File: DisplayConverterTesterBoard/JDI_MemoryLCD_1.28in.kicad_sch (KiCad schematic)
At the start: 6 parts, among them J6 Conn_01x03, J7 Conn_01x10_MountingPin

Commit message: set components LCSC
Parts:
- C? (x2): footprint (none) -> Capacitor_SMD:C_0805_2012Metric_Pad1.18x1.45mm_HandSolder; LCSC (none) -> C1853551; Vendor (none) -> YAGEO(国巨); Vendor Model (none) -> CC0805JKX7R0BB104
- C?: footprint (none) -> Resistor_SMD:R_0805_2012Metric_Pad1.20x1.40mm_HandSolder; LCSC (none) -> C28323; Vendor (none) -> SAMSUNG(三星); Vendor Model (none) -> CL21B105KBFNNNE
- NT2: footprint (none) -> NetTie:NetTie-3_SMD_Pad0.5mm
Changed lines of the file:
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@@
       (effects (font (size 1.27 1.27)) (justify left))
     )
-    (property "Footprint" "" (at 143.2052 138.43 0)
+    (property "Footprint" "Capacitor_SMD:C_0805_2012Metric_Pad1.18x1.45mm_HandSolder" (at 143.2052 138.43 0)
       (effects (font (size 1.27 1.27)) hide)
     )
     (property "Datasheet" "~" (at 142.24 134.62 0)
+      (effects (font (size 1.27 1.27)) hide)
+    )
+    (property "Description" "容值: 100nF 精度: ±5% 额定电压: 100V 材质(温度系数): X7R " (at 142.24 134.62 0)
+      (effects (font (size 1.27 1.27)) hide)
+    )
+    (property "LCSC" "C1853551" (at 142.24 134.62 0)
+      (effects (font (size 1.27 1.27)) hide)
+    )
+    (property "Vendor" "YAGEO(国巨)" (at 142.24 134.62 0)
+      (effects (font (size 1.27 1.27)) hide)
+    )
+    (property "Vendor Model" "CC0805JKX7R0BB104" (at 142.24 134.62 0)
       (effects (font (size 1.27 1.27)) hide)
     )
@@
       (effects (font (size 1.27 1.27)))
     )
-    (property "Footprint" "" (at 140.97 170.18 0)
+    (property "Footprint" "NetTie:NetTie-3_SMD_Pad0.5mm" (at 140.97 170.18 0)
       (effects (font (size 1.27 1.27)) hide)
     )
@@
       (effects (font (size 1.27 1.27)) hide)
     )
+    (property "Description" "" (at 140.97 170.18 0)
+      (effects (font (size 1.27 1.27)) hide)
+    )
+    (property "LCSC" "" (at 140.97 170.18 0)
+      (effects (font (size 1.27 1.27)) hide)
+    )
+    (property "Vendor" "" (at 140.97 170.18 0)
+      (effects (font (size 1.27 1.27)) hide)
+    )
+    (property "Vendor Model" "" (at 140.97 170.18 0)
+      (effects (font (size 1.27 1.27)) hide)
+    )
     (pin "1")
     (pin "2")
@@
     )
     (property "Datasheet" "~" (at 67.31 83.82 0)
+      (effects (font (size 1.27 1.27)) hide)
+    )
+    (property "Description" "" (at 67.31 83.82 0)
+      (effects (font (size 1.27 1.27)) hide)
+    )
+    (property "LCSC" "" (at 67.31 83.82 0)
+      (effects (font (size 1.27 1.27)) hide)
+    )
+    (property "Vendor" "" (at 67.31 83.82 0)
+      (effects (font (size 1.27 1.27)) hide)
+    )
+    (property "Vendor Model" "" (at 67.31 83.82 0)
       (effects (font (size 1.27 1.27)) hide)
     )
@@
       (effects (font (size 1.27 1.27)) (justify left))
     )
-    (property "Footprint" "" (at 159.7152 138.43 0)
+    (property "Footprint" "Capacitor_SMD:C_0805_2012Metric_Pad1.18x1.45mm_HandSolder" (at 159.7152 138.43 0)
       (effects (font (size 1.27 1.27)) hide)
     )
     (property "Datasheet" "~" (at 158.75 134.62 0)
+      (effects (font (size 1.27 1.27)) hide)
+    )
+    (property "Description" "容值: 100nF 精度: ±5% 额定电压: 100V 材质(温度系数): X7R " (at 158.75 134.62 0)
+      (effects (font (size 1.27 1.27)) hide)
+    )
+    (property "LCSC" "C1853551" (at 158.75 134.62 0)
+      (effects (font (size 1.27 1.27)) hide)
+    )
+    (property "Vendor" "YAGEO(国巨)" (at 158.75 134.62 0)
+      (effects (font (size 1.27 1.27)) hide)
+    )
+    (property "Vendor Model" "CC0805JKX7R0BB104" (at 158.75 134.62 0)
       (effects (font (size 1.27 1.27)) hide)
     )
@@
     )
     (property "Datasheet" "~" (at 132.08 82.55 0)
+      (effects (font (size 1.27 1.27)) hide)
+    )
+    (property "Description" "" (at 132.08 82.55 0)
+      (effects (font (size 1.27 1.27)) hide)
+    )
+    (property "LCSC" "" (at 132.08 82.55 0)
+      (effects (font (size 1.27 1.27)) hide)
+    )
+    (property "Vendor" "" (at 132.08 82.55 0)
+      (effects (font (size 1.27 1.27)) hide)
+    )
+    (property "Vendor Model" "" (at 132.08 82.55 0)
       (effects (font (size 1.27 1.27)) hide)
     )
@@
       (effects (font (size 1.27 1.27)) (justify left))
     )
-    (property "Footprint" "" (at 124.7648 138.43 0)
+    (property "Footprint" "Resistor_SMD:R_0805_2012Metric_Pad1.20x1.40mm_HandSolder" (at 124.7648 138.43 0)
       (effects (font (size 1.27 1.27)) hide)
     )
@@
       (effects (font (size 1.27 1.27)) hide)
     )
+    (property "Description" "容值: 1uF 精度: ±10% 额定电压: 50V 材质(温度系数): X7R 材质:X7R" (at 125.73 134.62 0)
+      (effects (font (size 1.27 1.27)) hide)
+    )
+    (property "LCSC" "C28323" (at 125.73 134.62 0)
+      (effects (font (size 1.27 1.27)) hide)
+    )
+    (property "Vendor" "SAMSUNG(三星)" (at 125.73 134.62 0)
+      (effects (font (size 1.27 1.27)) hide)
+    )
+    (property "Vendor Model" "CL21B105KBFNNNE" (at 125.73 134.62 0)
+      (effects (font (size 1.27 1.27)) hide)
+    )

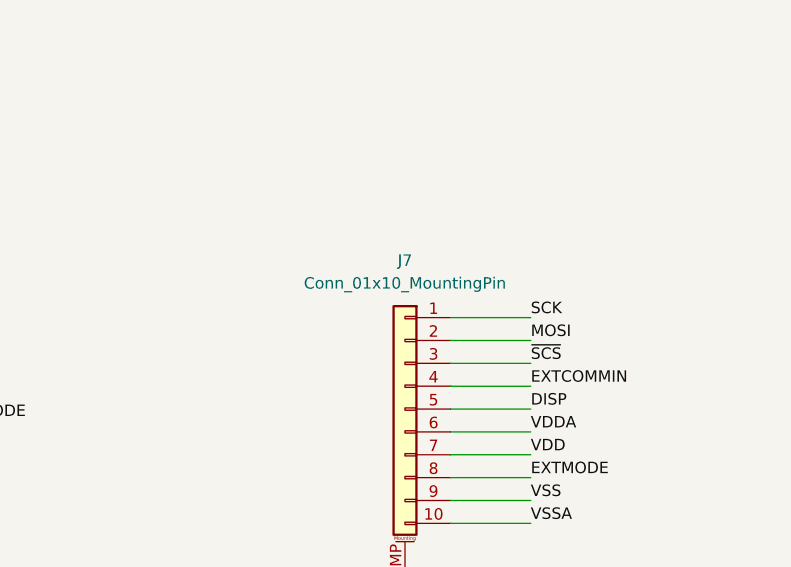
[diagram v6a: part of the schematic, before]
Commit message: updated FPC connectors
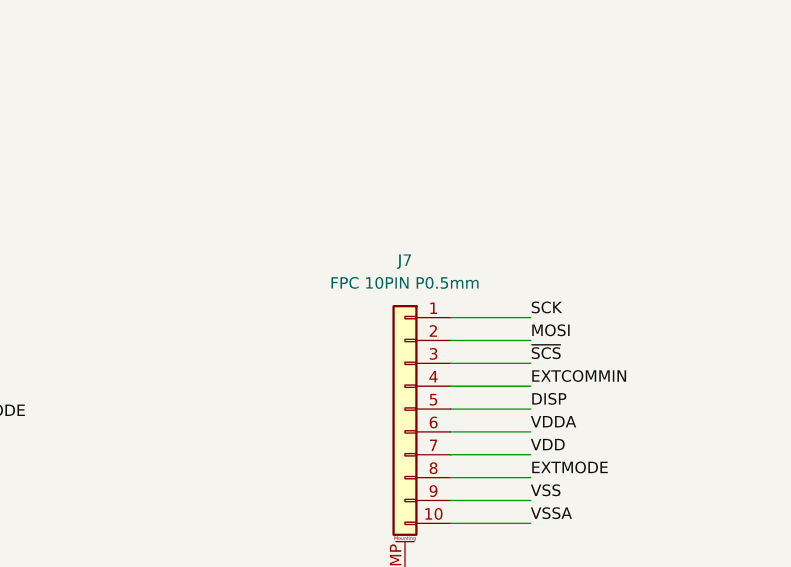
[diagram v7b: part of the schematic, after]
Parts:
- J7: value Conn_01x10_MountingPin -> FPC 10PIN P0.5mm; footprint Connector_FFC-FPC:Hirose_FH12-10S-0.5SH_1x10-1MP_P0.50mm_Horizontal -> IotPi_Connector_FPC:Kinghelm_KH-FPC0.5-H1.0SMT-10P-QCHF; LCSC (none) -> C3250114; Vendor (none) -> kinghelm(金航标); Vendor Model (none) -> KH-FPC0.5-H1.0SMT-10P-
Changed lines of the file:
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@@
       (effects (font (size 1.27 1.27)))
     )
-    (property "Value" "Conn_01x10_MountingPin" (at 132.08 68.58 0)
+    (property "Value" "FPC 10PIN P0.5mm" (at 132.08 68.58 0)
       (effects (font (size 1.27 1.27)))
     )
-    (property "Footprint" "Connector_FFC-FPC:Hirose_FH12-10S-0.5SH_1x10-1MP_P0.50mm_Horizontal" (at 132.08 82.55 0)
+    (property "Footprint" "IotPi_Connector_FPC:Kinghelm_KH-FPC0.5-H1.0SMT-10P-QCHF" (at 132.08 82.55 0)
       (effects (font (size 1.27 1.27)) hide)
     )
@@
       (effects (font (size 1.27 1.27)) hide)
     )
-    (property "LCSC" "" (at 132.08 82.55 0)
+    (property "LCSC" "C3250114" (at 132.08 82.55 0)
       (effects (font (size 1.27 1.27)) hide)
     )
-    (property "Vendor" "" (at 132.08 82.55 0)
+    (property "Vendor" "kinghelm(金航标)" (at 132.08 82.55 0)
       (effects (font (size 1.27 1.27)) hide)
     )
-    (property "Vendor Model" "" (at 132.08 82.55 0)
+    (property "Vendor Model" "KH-FPC0.5-H1.0SMT-10P-" (at 132.08 82.55 0)
       (effects (font (size 1.27 1.27)) hide)
     )

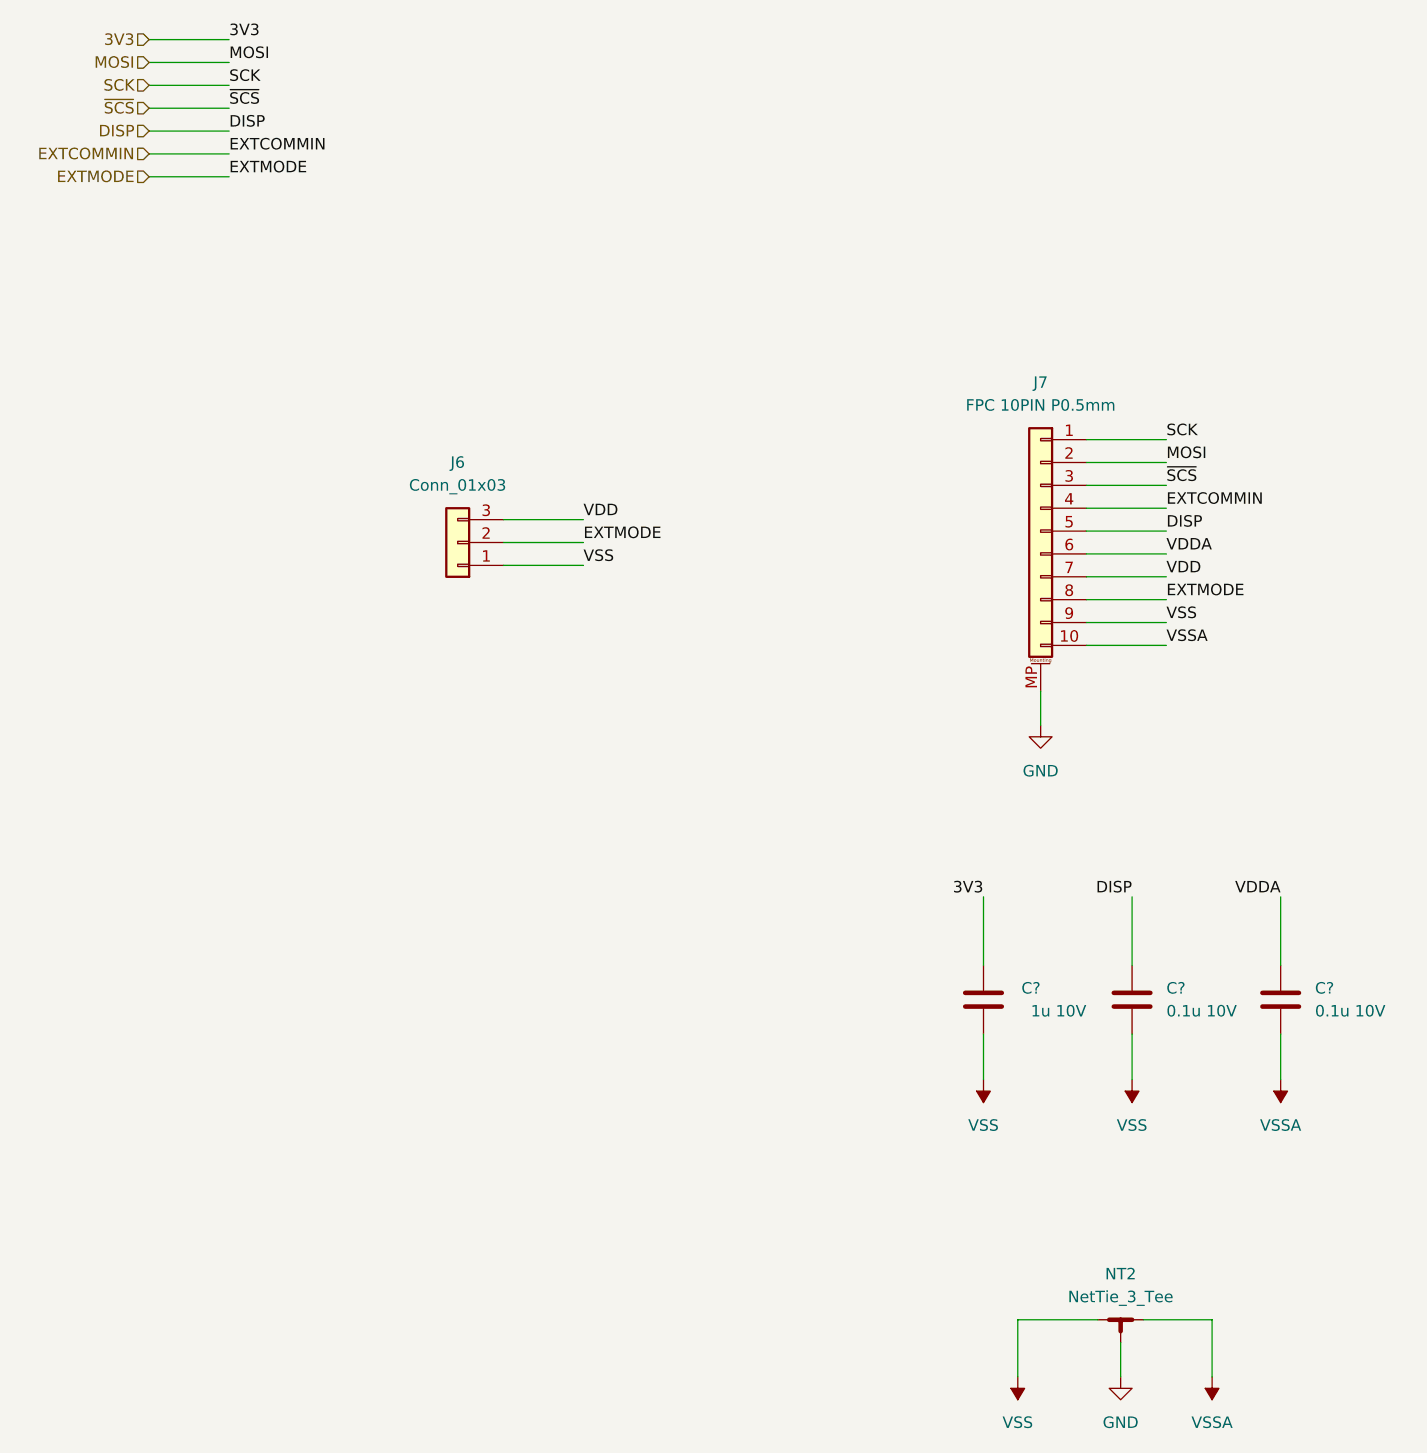
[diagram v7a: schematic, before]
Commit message: updated layout
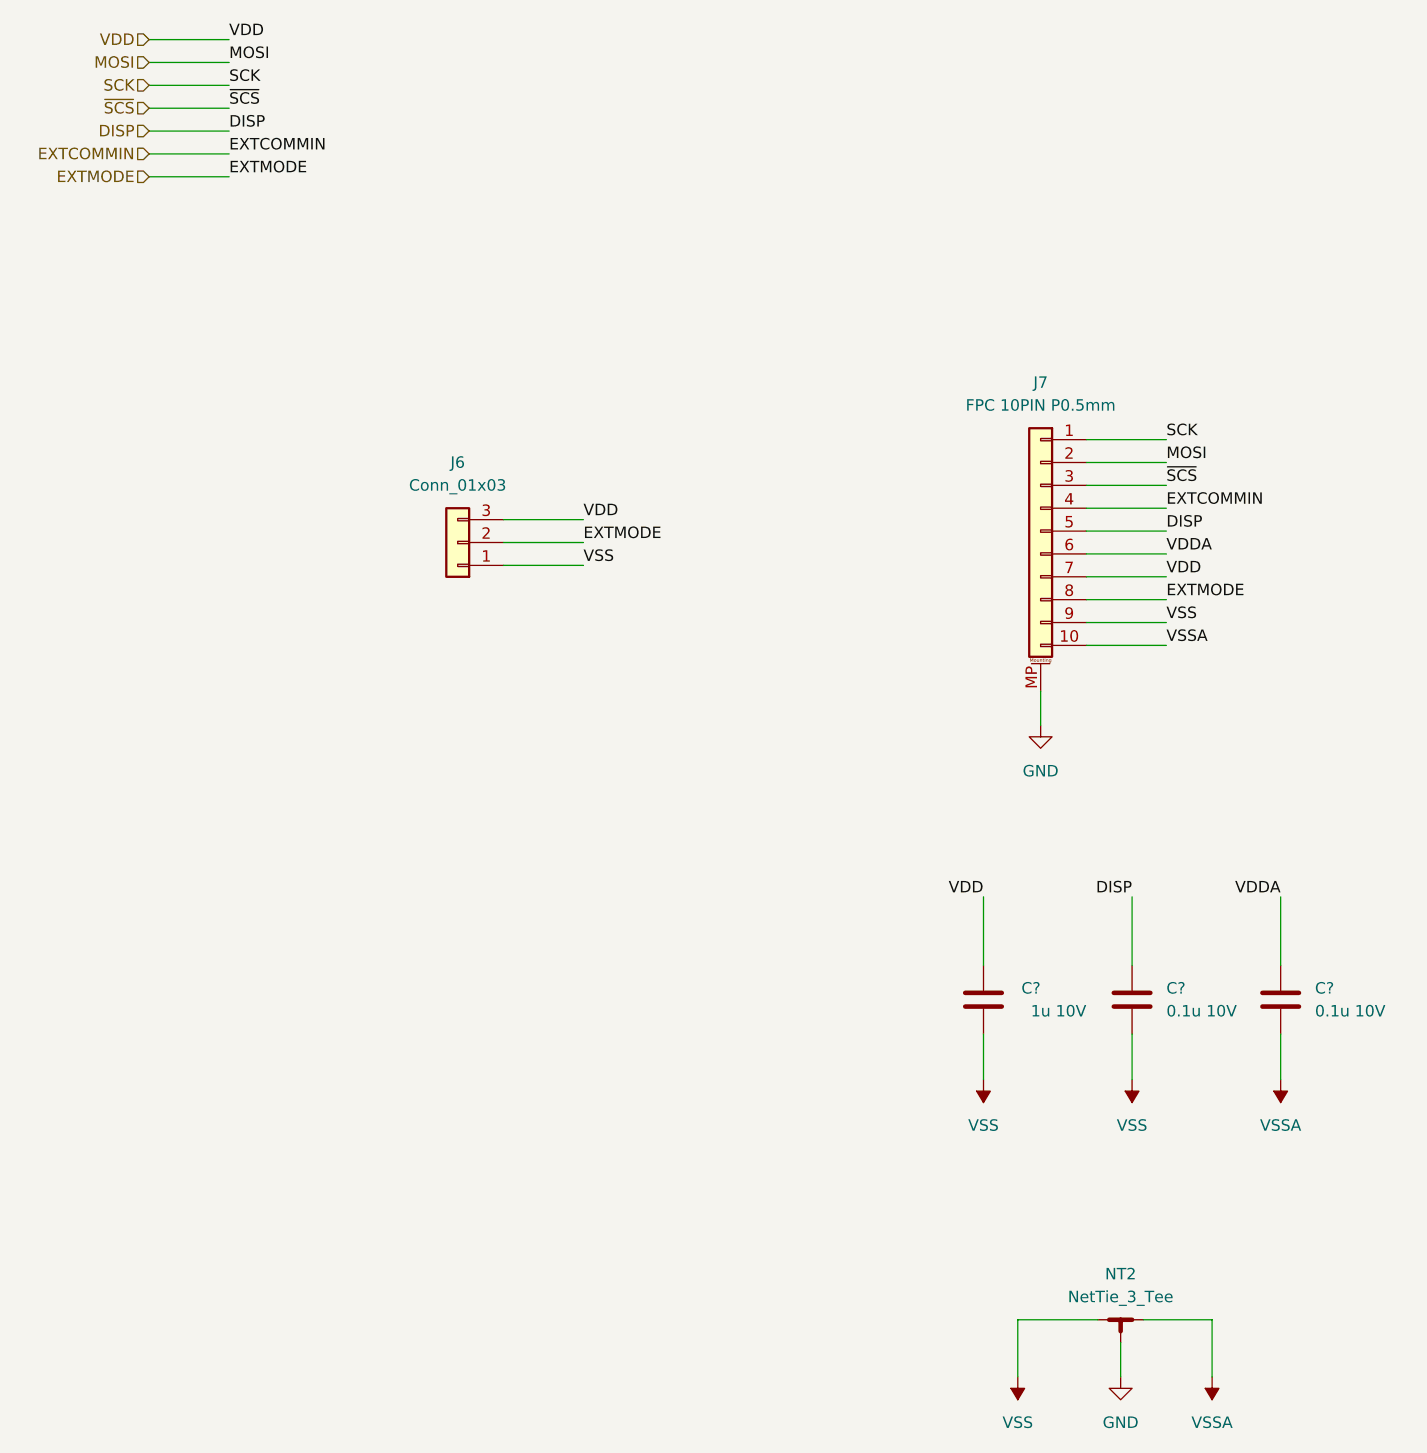
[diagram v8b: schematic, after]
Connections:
- net 3V3 is gone; now on net VDD: C?.1
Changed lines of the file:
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@@
     (effects (font (size 1.27 1.27)) (justify left bottom))
   )
-  (label "3V3" (at 41.91 27.94 0) (fields_autoplaced)
+  (label "VDD" (at 41.91 27.94 0) (fields_autoplaced)
     (effects (font (size 1.27 1.27)) (justify left bottom))
   )
@@
     (effects (font (size 1.27 1.27)) (justify left bottom))
   )
-  (label "3V3" (at 125.73 123.19 180) (fields_autoplaced)
+  (label "VDD" (at 125.73 123.19 180) (fields_autoplaced)
     (effects (font (size 1.27 1.27)) (justify right bottom))
   )
@@
     (effects (font (size 1.27 1.27)) (justify right))
   )
-  (hierarchical_label "3V3" (shape input) (at 33.02 27.94 180) (fields_autoplaced)
+  (hierarchical_label "VDD" (shape input) (at 33.02 27.94 180) (fields_autoplaced)
     (effects (font (size 1.27 1.27)) (justify right))
   )
